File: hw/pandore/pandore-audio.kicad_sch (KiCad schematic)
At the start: 15 parts, among them J28 AUDIO.D-, J29 AUDIO.D+, U33 5.5V 1A, U9 Teensy 4.1

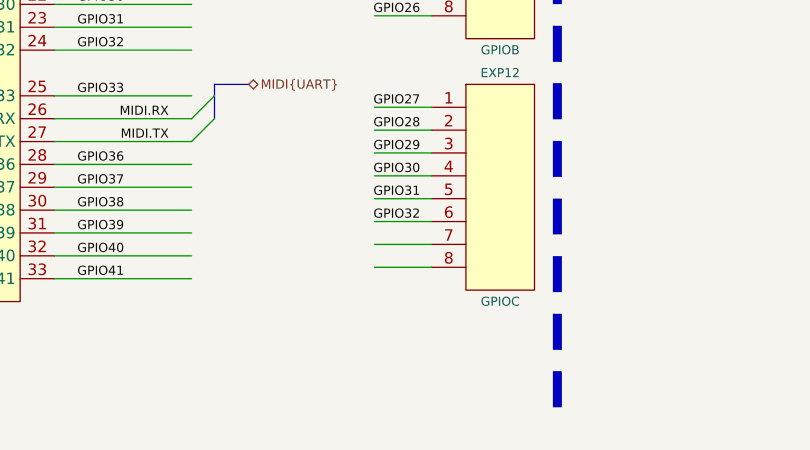
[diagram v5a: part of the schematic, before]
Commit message: finished adding mpn,mfg to all parts, finished routing placement
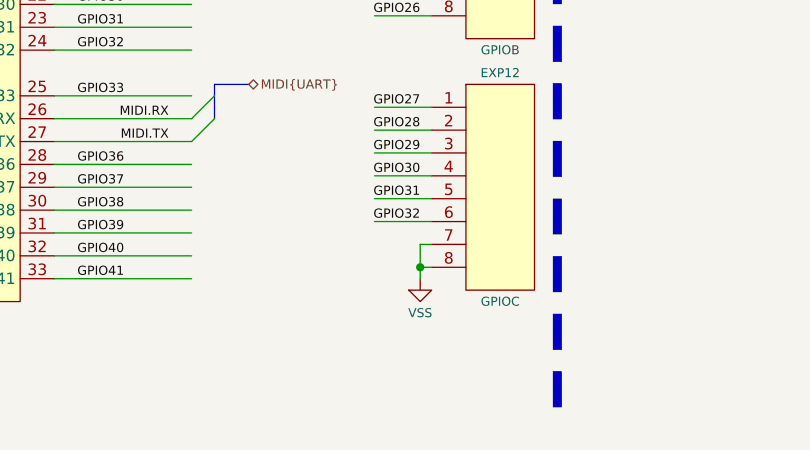
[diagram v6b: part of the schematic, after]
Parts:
- C263, C264: MFG (none) -> KEMET; MPN (none) -> C0603C105K4RACTU
- EXP10, EXP11, EXP12, EXP13: Link url-link -> (none); MFG MFG -> Amphenol ICC (FCI); MPN MPN -> 10129378-908002BLF
- JMP6, JMP7: MFG (none) -> Adam Tech; MPN (none) -> PH1-02-UA
- R202, R203: Link (none) -> https://yageogroup.com/products/Resistors/part/RC0402JR-070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; MFG (none) -> Yageo; MFG2 (none) -> Stackpole; MFG3 (none) -> Vishay Dale; MPN (none) -> RC0402JR-070RL; MPN2 (none) -> RMCF0402ZT0R00; MPN3 (none) -> CRCW04020000Z0ED
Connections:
- net VSS: now also EXP12.7, EXP12.8
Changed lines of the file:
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@@
 	)
 	(junction
+		(at 156.21 180.34)
+		(diameter 0)
+		(color 0 0 0 0)
+	)
+	(junction
 		(at 55.88 74.93)
 		(diameter 0)
@@
 	(wire
 		(pts
-			(xy 151.13 177.8) (xy 157.48 177.8)
+			(xy 156.21 177.8) (xy 157.48 177.8)
 		)
 		(stroke
@@
 	(wire
 		(pts
-			(xy 151.13 180.34) (xy 157.48 180.34)
-		)
-		(stroke
-			(width 0)
-			(type default)
-		)
-	)
-	(wire
-		(pts
 			(xy 115.57 166.37) (xy 130.81 166.37)
 		)
@@
 	(wire
 		(pts
+			(xy 156.21 177.8) (xy 156.21 180.34)
+		)
+		(stroke
+			(width 0)
+			(type default)
+		)
+	)
+	(wire
+		(pts
 			(xy 55.88 88.9) (xy 55.88 87.63)
 		)
@@
 		)
 	)
+	(wire
+		(pts
+			(xy 156.21 180.34) (xy 157.48 180.34)
+		)
+		(stroke
+			(width 0)
+			(type default)
+		)
+	)
 	(bus
 		(pts
@@
 	(wire
 		(pts
+			(xy 156.21 180.34) (xy 156.21 181.61)
+		)
+		(stroke
+			(width 0)
+			(type default)
+		)
+	)
+	(wire
+		(pts
 			(xy 151.13 116.84) (xy 157.48 116.84)
 		)
@@
 			)
 		)
-		(property "Datasheet" "url-ds"
+		(property "Datasheet" "https://www.waldom.com/productfiles/mf-FCI/10129378-908002BLF.pdf"
 			(at 165.1 135.636 0)
 			(do_not_autoplace yes)
@@
 			)
 		)
-		(property "MPN" "MPN"
+		(property "MPN" "10129378-908002BLF"
 			(at 165.1 129.794 0)
 			(do_not_autoplace yes)
@@
 			)
 		)
-		(property "MFG" "MFG"
+		(property "MFG" "Amphenol ICC (FCI)"
 			(at 171.704 129.794 0)
 			(do_not_autoplace yes)
@@
 			)
 		)
-		(property "Link" "url-link"
+		(property "Link" ""
 			(at 165.1 134.366 0)
 			(do_not_autoplace yes)
@@
 			)
 		)
-		(property "Datasheet" "url-ds"
+		(property "Datasheet" "https://www.waldom.com/productfiles/mf-FCI/10129378-908002BLF.pdf"
 			(at 165.1 163.576 0)
 			(do_not_autoplace yes)
@@
 			)
 		)
-		(property "MPN" "MPN"
+		(property "MPN" "10129378-908002BLF"
 			(at 165.1 157.734 0)
 			(do_not_autoplace yes)
@@
 			)
 		)
-		(property "MFG" "MFG"
+		(property "MFG" "Amphenol ICC (FCI)"
 			(at 171.704 157.734 0)
 			(do_not_autoplace yes)
@@
 			)
 		)
-		(property "Link" "url-link"
+		(property "Link" ""
 			(at 165.1 162.306 0)
 			(do_not_autoplace yes)
@@
 			)
 		)
-		(property "Datasheet" "url-ds"
+		(property "Datasheet" "https://www.waldom.com/productfiles/mf-FCI/10129378-908002BLF.pdf"
 			(at 48.26 191.516 0)
 			(do_not_autoplace yes)
@@
 			)
 		)
-		(property "MPN" "MPN"
+		(property "MPN" "10129378-908002BLF"
 			(at 48.26 185.674 0)
 			(do_not_autoplace yes)
@@
 			)
 		)
-		(property "MFG" "MFG"
+		(property "MFG" "Amphenol ICC (FCI)"
 			(at 54.864 185.674 0)
 			(do_not_autoplace yes)
@@
 			)
 		)
-		(property "Link" "url-link"
+		(property "Link" ""
 			(at 48.26 190.246 0)
 			(do_not_autoplace yes)
@@
 			)
 		)
-		(property "Datasheet" "url-ds"
+		(property "Datasheet" "https://www.waldom.com/productfiles/mf-FCI/10129378-908002BLF.pdf"
 			(at 165.1 191.516 0)
 			(do_not_autoplace yes)
@@
 			)
 		)
-		(property "MPN" "MPN"
+		(property "MPN" "10129378-908002BLF"
 			(at 165.1 185.674 0)
 			(do_not_autoplace yes)
@@
 			)
 		)
-		(property "MFG" "MFG"
+		(property "MFG" "Amphenol ICC (FCI)"
 			(at 171.704 185.674 0)
 			(do_not_autoplace yes)
@@
 			)
 		)
-		(property "Link" "url-link"
+		(property "Link" ""
 			(at 165.1 190.246 0)
 			(do_not_autoplace yes)
@@
 			)
 		)
-		(property "Datasheet" ""
+		(property "Datasheet" "https://yageogroup.com/component-documentation/download/specsheet/RC0402JR-070RL"
 			(at 50.546 119.38 0)
 			(do_not_autoplace yes)
@@
 			)
 		)
-		(property "MPN" ""
+		(property "MPN" "RC0402JR-070RL"
 			(at 46.99 119.38 0)
 			(do_not_autoplace yes)
@@
 			)
 		)
-		(property "MFG" ""
+		(property "MFG" "Yageo"
 			(at 47.244 133.35 0)
 			(do_not_autoplace yes)
@@
 			)
 		)
-		(property "Link" ""
+		(property "Link" "https://yageogroup.com/products/Resistors/part/RC0402JR-070RL"
 			(at 49.022 119.634 0)
 			(do_not_autoplace yes)
@@
 			)
 		)
-		(property "MPN2" ""
+		(property "MPN2" "RMCF0402ZT0R00"
 			(at 45.212 118.872 0)
 			(do_not_autoplace yes)
@@
 			)
 		)
-		(property "MFG2" ""
+		(property "MFG2" "Stackpole"
 			(at 45.212 133.604 0)
 			(do_not_autoplace yes)
@@
 			)
 		)
-		(property "MPN3" ""
+		(property "MPN3" "CRCW04020000Z0ED"
 			(at 43.434 119.38 0)
 			(do_not_autoplace yes)
@@
 			)
 		)
-		(property "MFG3" ""
+		(property "MFG3" "Vishay Dale"
 			(at 43.434 133.604 0)
 			(do_not_autoplace yes)
@@
 			)
 		)
-		(property "Datasheet" ""
+		(property "Datasheet" "https://app.adam-tech.com/products/download/data_sheet/201605/ph1-xx-ua-data-sheet.pdf"
 			(at 61.976 19.05 0)
 			(do_not_autoplace yes)
@@
 			)
 		)
-		(property "MPN" ""
+		(property "MPN" "PH1-02-UA"
 			(at 56.134 19.05 0)
 			(do_not_autoplace yes)
@@
 			)
 		)
-		(property "MFG" ""
+		(property "MFG" "Adam Tech"
 			(at 56.134 12.446 0)
 			(do_not_autoplace yes)
@@
 			)
 		)
-		(property "Datasheet" ""
+		(property "Datasheet" "https://yageogroup.com/content/datasheet/asset/file/KEM_C1002_X7R_SMD"
 			(at 25.4 89.408 0)
 			(do_not_autoplace yes)
@@
 			)
 		)
-		(property "MPN" ""
+		(property "MPN" "C0603C105K4RACTU"
 			(at 25.4 93.726 0)
 			(do_not_autoplace yes)
@@
 			)
 		)
-		(property "MFG" ""
+		(property "MFG" "KEMET"
 			(at 13.462 93.726 0)
 			(do_not_autoplace yes)
@@
 			)
 		)
-		(property "Datasheet" ""
+		(property "Datasheet" "https://yageogroup.com/component-documentation/download/specsheet/RC0402JR-070RL"
 			(at 50.546 116.84 0)
 			(do_not_autoplace yes)
@@
 			)
 		)
-		(property "MPN" ""
+		(property "MPN" "RC0402JR-070RL"
 			(at 46.99 116.84 0)
 			(do_not_autoplace yes)
@@
 			)
 		)
-		(property "MFG" ""
+		(property "MFG" "Yageo"
 			(at 47.244 130.81 0)
 			(do_not_autoplace yes)
@@
 			)
 		)
-		(property "Link" ""
+		(property "Link" "https://yageogroup.com/products/Resistors/part/RC0402JR-070RL"
 			(at 49.022 117.094 0)
 			(do_not_autoplace yes)
@@
 			)
 		)
-		(property "MPN2" ""
+		(property "MPN2" "RMCF0402ZT0R00"
 			(at 45.212 116.332 0)
 			(do_not_autoplace yes)
@@
 			)
 		)
-		(property "MFG2" ""
+		(property "MFG2" "Stackpole"
 			(at 45.212 131.064 0)
 			(do_not_autoplace yes)
@@
 			)
 		)
-		(property "MPN3" ""
+		(property "MPN3" "CRCW04020000Z0ED"
 			(at 43.434 116.84 0)
 			(do_not_autoplace yes)
@@
 			)
 		)
-		(property "MFG3" ""
+		(property "MFG3" "Vishay Dale"
 			(at 43.434 131.064 0)
 			(do_not_autoplace yes)
@@
 			)
 		)
-		(property "Datasheet" ""
+		(property "Datasheet" "https://yageogroup.com/content/datasheet/asset/file/KEM_C1002_X7R_SMD"
 			(at 55.88 93.218 0)
 			(do_not_autoplace yes)
@@
 			)
 		)
-		(property "MPN" ""
+		(property "MPN" "C0603C105K4RACTU"
 			(at 55.88 97.536 0)
 			(do_not_autoplace yes)
@@
 			)
 		)
-		(property "MFG" ""
+		(property "MFG" "KEMET"
 			(at 67.818 97.536 0)
 			(do_not_autoplace yes)
@@
 			)
 		)
-		(property "Datasheet" ""
+		(property "Datasheet" "https://app.adam-tech.com/products/download/data_sheet/201605/ph1-xx-ua-data-sheet.pdf"
 			(at 61.976 39.37 0)
 			(do_not_autoplace yes)
@@
 			)
 		)
-		(property "MPN" ""
+		(property "MPN" "PH1-02-UA"
 			(at 56.134 39.37 0)
 			(do_not_autoplace yes)
@@
 			)
 		)
-		(property "MFG" ""
+		(property "MFG" "Adam Tech"
 			(at 56.134 45.974 0)
 			(do_not_autoplace yes)
@@
 					(unit 1)
 				)
+			)
+		)
+	)
+	(symbol
+		(lib_id "reekilib_pwr:VSS")
+		(at 156.21 182.88 0)
+		(unit 1)
+		(exclude_from_sim no)
+		(in_bom no)
+		(on_board no)
+		(dnp no)
+		(property "Reference" "#PWR0391"
+			(at 156.21 187.325 0)
+			(do_not_autoplace yes)
+			(effects
+				(font
+					(size 1 1)
+				)
+				(hide yes)
+			)
+		)
+		(property "Value" "VSS"
+			(at 156.21 185.42 0)
+			(effects
+				(font
+					(size 1 1)
+				)
+			)
+		)
+		(property "Footprint" ""
+			(at 156.21 182.88 0)
+			(effects
+				(font
+					(size 1.524 1.524)
+				)
+			)
+		)
+		(property "Datasheet" ""
+			(at 156.21 180.34 0)
+			(effects
+				(font
+					(size 1.524 1.524)
+				)
+			)
+		)
+		(property "Description" ""
+			(at 156.21 182.88 0)
+			(effects
+				(font
+					(size 1.27 1.27)
+				)
+				(hide yes)
+			)
+		)
+		(pin "1"
+		)
+		(instances
+			(project "pandore"
+				(path "/e55f2700-f75a-4062-8a27-fe258faa8966/b4e2772d-7748-46ec-bd38-bc8e72cebcb8"
+					(reference "#PWR0391")
+					(unit 1)
+				)
